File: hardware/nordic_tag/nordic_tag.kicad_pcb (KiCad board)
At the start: 2 copper layers, 85.1 x 43.2 mm, 39 parts, among them J101 USB_B_Micro, J102 Conn_01x08_Male, SW201 SW_Push, SW301 SW_Push, SW302 SW_Push, U101 AP2112K-3.3, U201 nRF52811-QCAA, U301 STM32F042F4Px, Y201 32MHz, Y301 32MHz

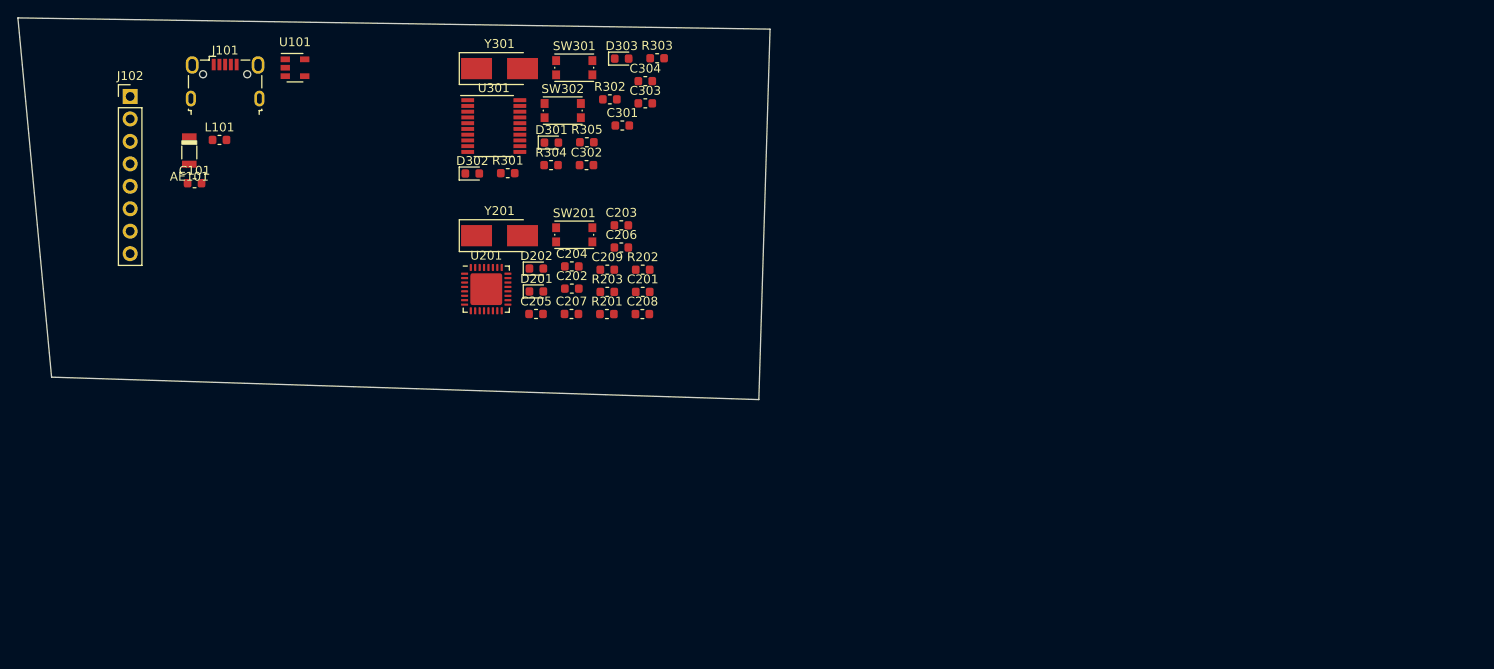
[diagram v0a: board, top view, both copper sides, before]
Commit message: Switched to pcb antenna. started placement
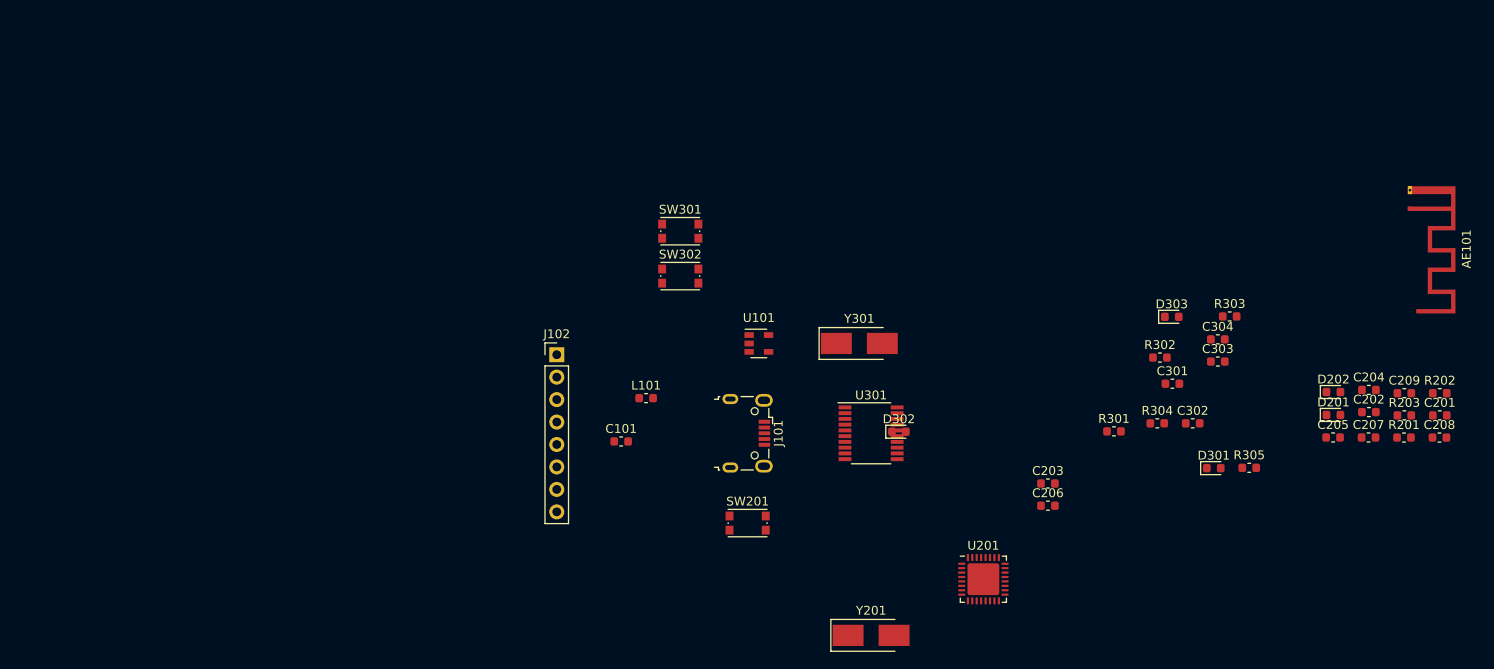
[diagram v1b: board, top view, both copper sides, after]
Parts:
- AE101: value Antenna_Chip -> Antenna_Shield; footprint nordic_tag:RFANT3216120A5T -> RF_Antenna:Texas_SWRA117D_2.4GHz_Right
- Y301: value 32MHz -> 8MHz
- moved AE101 138.2 mm to (214.6, 83.8), turned to 270 degrees
- moved C202 91.2 mm to (210.0, 106.8)
- moved C204 91.2 mm to (210.0, 104.3)
- moved R201 91.2 mm to (214.0, 109.7)
- moved C205 91.2 mm to (205.9, 109.7)
- moved C208 91.2 mm to (218.0, 109.7)
- moved C209 91.2 mm to (214.0, 104.7)
- moved R203 91.2 mm to (214.0, 107.2)
- moved C201 91.2 mm to (218.0, 107.2)
- moved C207 91.2 mm to (209.9, 109.7)
- moved D201 91.2 mm to (206.0, 107.1)
- moved D202 91.2 mm to (206.0, 104.6)
- moved R202 91.2 mm to (218.0, 104.7)
- moved D301 83.5 mm to (192.4, 113.2)
- moved R305 83.5 mm to (196.4, 113.1)
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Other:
- board outline removed
- net class Power added: clearance 0.2, trace_width 0.381, via_dia 0.8, via_drill 0.4
- net class RF added: clearance 0.2, trace_width 0.29337, via_dia 0.8, via_drill 0.4
